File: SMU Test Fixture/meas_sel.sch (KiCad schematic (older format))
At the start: 4 parts, among them K34 6x1 Mux Sel A, K35 6x1 Mux Sel B, K36 6x1 Mux Sel C, K37 6x1 Mux Sel C

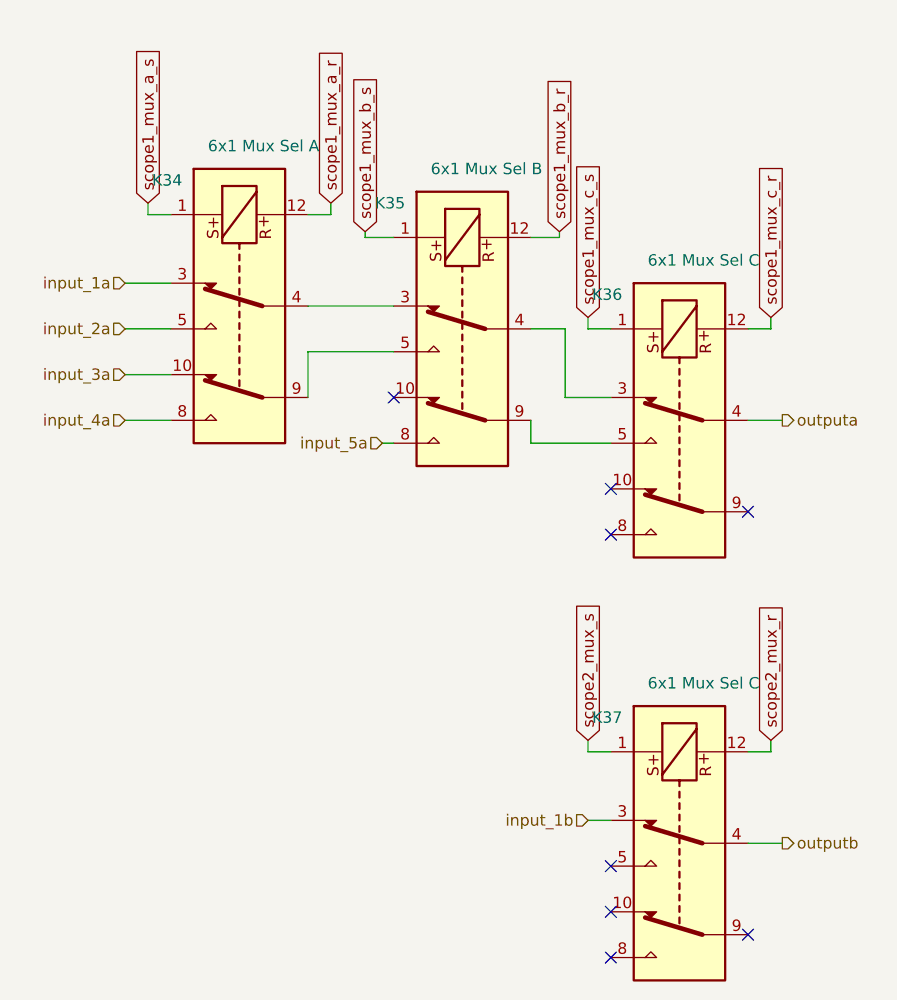
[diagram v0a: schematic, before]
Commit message: Elminate extra scope cal relay, re-organize relays, re-annotate, ERC
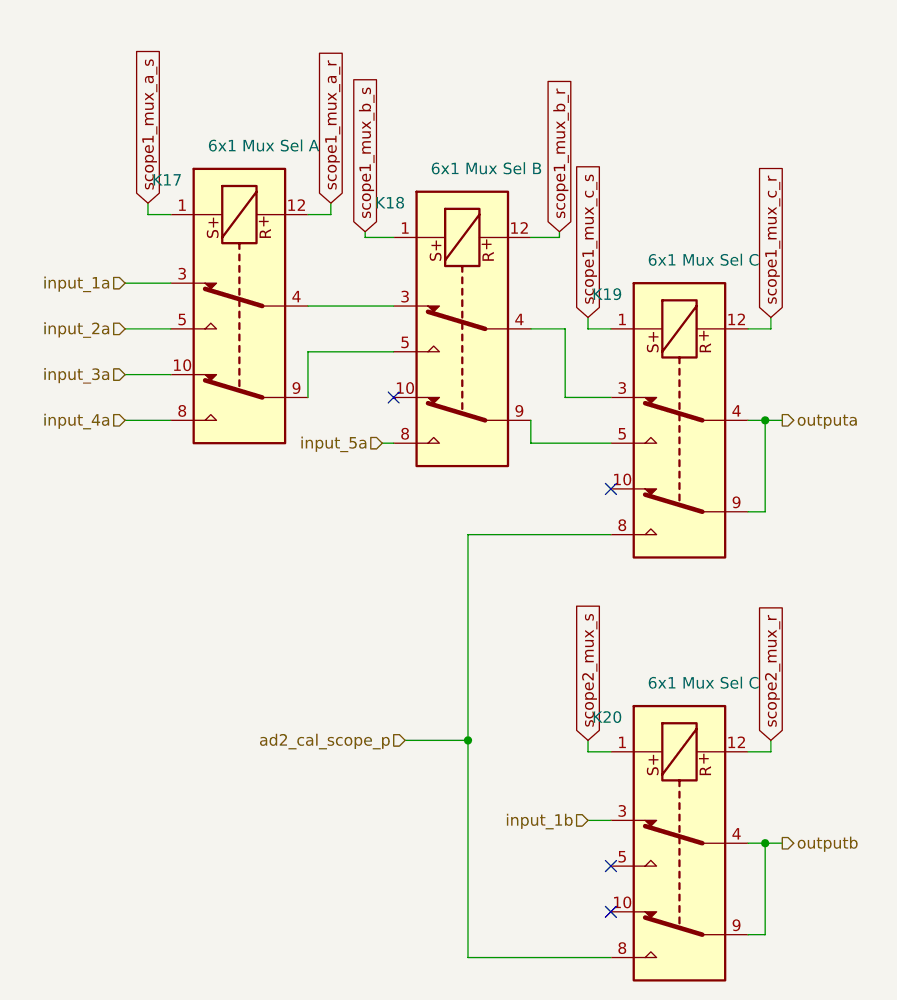
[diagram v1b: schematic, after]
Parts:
- renumbered K34 to K17, K35 to K18, K36 to K19, K37 to K20
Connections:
- net outputa: now also K19.9
- net outputb: now also K20.9
- net ad2_cal_scope_p: now reaches K19.8
- net ad2_cal_scope_p: now also K20.8
- no-connect marks 8 -> 4
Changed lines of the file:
@@
 $Descr A4 11693 8268
 encoding utf-8
-Sheet 7 8
+Sheet 6 8
 Title ""
 Date ""
@@
 AR Path="/62B74232/5FC86CAB" Ref="K?"  Part="1"
 AR Path="/5FC86CAB" Ref="K?"  Part="1"
-AR Path="/5FC868AD/5FC86CAB" Ref="K36"  Part="1"
-F 0 "K36" V 6025 3150 50  0000 L CNN
+AR Path="/5FC868AD/5FC86CAB" Ref="K19"  Part="1"
+F 0 "K19" V 6025 3150 50  0000 L CNN
 F 1 "6x1 Mux Sel C" V 5875 2550 50  0000 L CNN
 F 2 "Relay_SMD:Relay_DPDT_Kemet_EE2_NUH" H 6575 2900 50  0001 C CNN
@@
 AR Path="/62B74232/5FC8A595" Ref="K?"  Part="1"
 AR Path="/5FC8A595" Ref="K?"  Part="1"
-AR Path="/5FC868AD/5FC8A595" Ref="K35"  Part="1"
-F 0 "K35" V 5075 2750 50  0000 L CNN
+AR Path="/5FC868AD/5FC8A595" Ref="K18"  Part="1"
+F 0 "K18" V 5075 2750 50  0000 L CNN
 F 1 "6x1 Mux Sel B" V 4925 2150 50  0000 L CNN
 F 2 "Relay_SMD:Relay_DPDT_Kemet_EE2_NUH" H 5625 2500 50  0001 C CNN
@@
 Text HLabel 7025 2900 2    50   Output ~ 0
 outputa
-NoConn ~ 6875 3300
 NoConn ~ 6275 3200
-NoConn ~ 6275 3400
 Wire Wire Line
 	4150 2300 4350 2300
@@
 	4150 2900 4350 2900
 Wire Wire Line
-	6875 2900 7025 2900
+	6875 2900 6950 2900
 Text GLabel 5200 2075 1    50   Input ~ 0
 scope1_mux_b_s
@@
 AR Path="/62B74232/60A4CED0" Ref="K?"  Part="1"
 AR Path="/60A4CED0" Ref="K?"  Part="1"
-AR Path="/5FC868AD/60A4CED0" Ref="K34"  Part="1"
-F 0 "K34" V 4100 2650 50  0000 L CNN
+AR Path="/5FC868AD/60A4CED0" Ref="K17"  Part="1"
+F 0 "K17" V 4100 2650 50  0000 L CNN
 F 1 "6x1 Mux Sel A" V 3950 2050 50  0000 L CNN
 F 2 "Relay_SMD:Relay_DPDT_Kemet_EE2_NUH" H 4650 2400 50  0001 C CNN
@@
 AR Path="/62B74232/60AE9270" Ref="K?"  Part="1"
 AR Path="/60AE9270" Ref="K?"  Part="1"
-AR Path="/5FC868AD/60AE9270" Ref="K37"  Part="1"
-F 0 "K37" V 6025 5000 50  0000 L CNN
+AR Path="/5FC868AD/60AE9270" Ref="K20"  Part="1"
+F 0 "K20" V 6025 5000 50  0000 L CNN
 F 1 "6x1 Mux Sel C" V 5875 4400 50  0000 L CNN
 F 2 "Relay_SMD:Relay_DPDT_Kemet_EE2_NUH" H 6575 4750 50  0001 C CNN
@@
 Text HLabel 7025 4750 2    50   Output ~ 0
 outputb
-NoConn ~ 6875 5150
 NoConn ~ 6275 5050
-NoConn ~ 6275 5250
-Wire Wire Line
-	6875 4750 7025 4750
+Wire Wire Line
+	6875 4750 6950 4750
 Text GLabel 6175 4300 1    50   Input ~ 0
 scope2_mux_s
@@
 Wire Wire Line
 	6175 4650 6275 4650
+Wire Wire Line
+	6950 2900 6950 3300
+Wire Wire Line
+	6950 3300 6875 3300
+Connection ~ 6950 2900
+Wire Wire Line
+	6950 2900 7025 2900
+Wire Wire Line
+	6950 4750 6950 5150
+Wire Wire Line
+	6950 5150 6875 5150
+Connection ~ 6950 4750
+Wire Wire Line
+	6950 4750 7025 4750
+Wire Wire Line
+	6275 3400 5650 3400
+Wire Wire Line
+	5650 3400 5650 4300
+Wire Wire Line
+	5650 5250 6275 5250
+Text HLabel 5375 4300 0    50   Input ~ 0
+ad2_cal_scope_p
+Wire Wire Line
+	5375 4300 5650 4300
+Connection ~ 5650 4300
+Wire Wire Line
+	5650 4300 5650 5250
 $EndSCHEMATC
